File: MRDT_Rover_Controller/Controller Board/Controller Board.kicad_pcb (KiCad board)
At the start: 2 copper layers, 137.6 x 81.5 mm, 31 parts, among them Q1 S8050, SW1 EG1218, U1 MCP3008

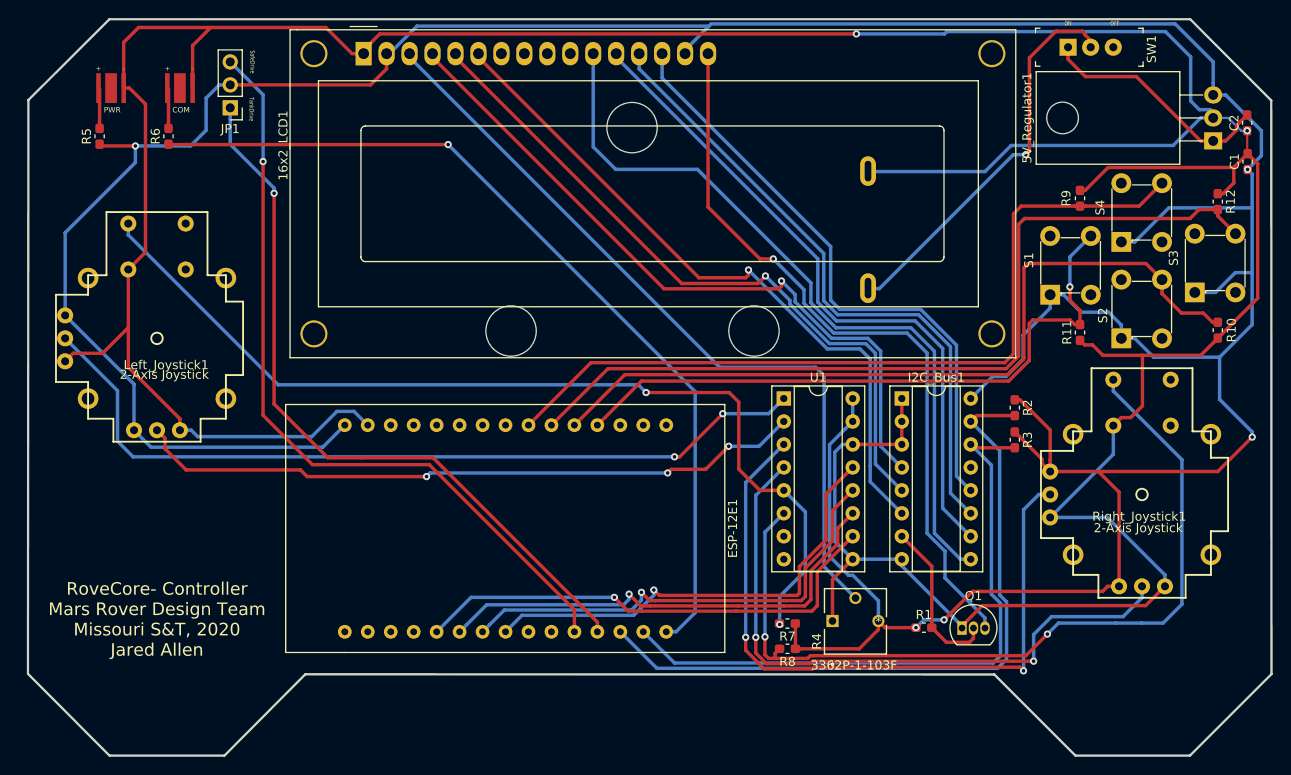
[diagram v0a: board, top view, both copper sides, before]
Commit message: All Push-Buttons Re-Mapped
Buttons 3 & 4 had to be re-mapped through the ADC due to compatability issues with the original pins they were connected to. All schematic and PCB changes have been made. Buttons 1 & 2 also needed to be re-mapped to account for the change, but are still connected to the ESP
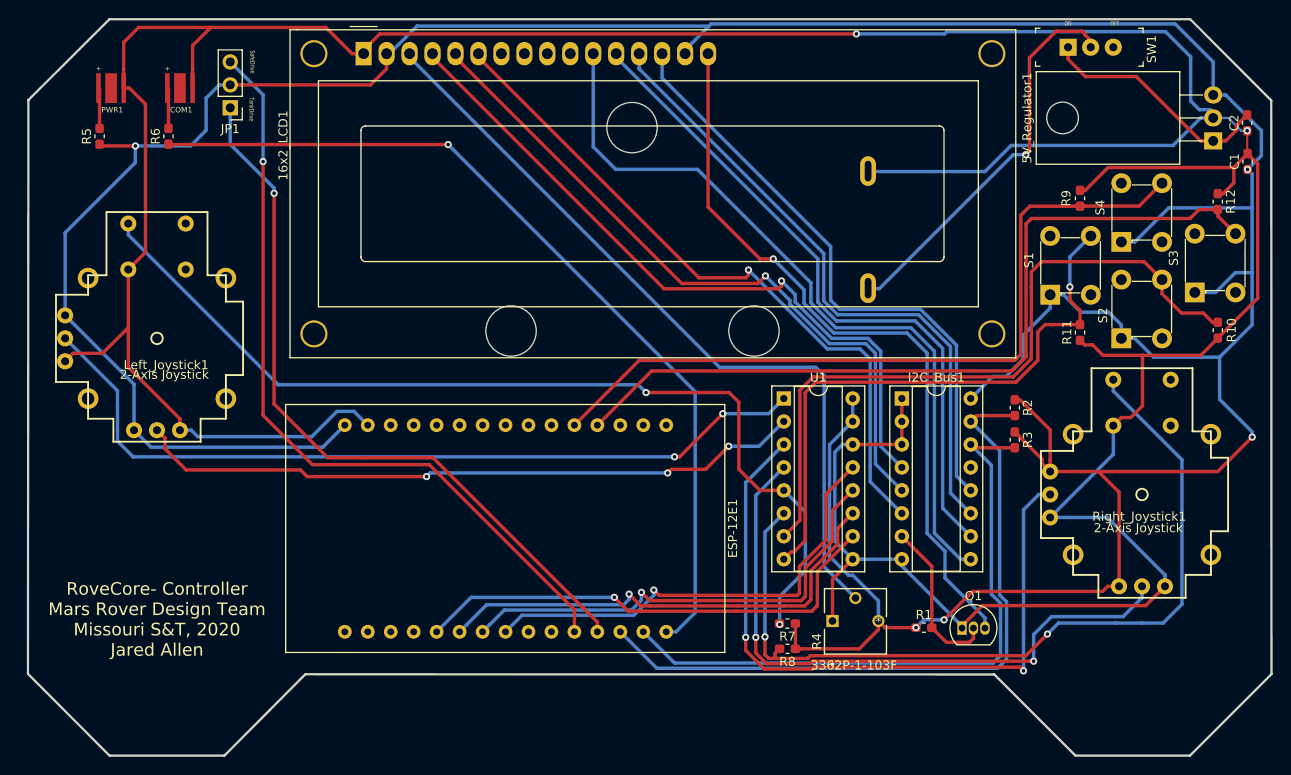
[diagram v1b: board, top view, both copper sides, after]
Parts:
- renumbered COM to COM1, PWR to PWR1
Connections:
- ESP-12E1 pad 11: SW3 -> Net-(ESP-12E1-Pad11)
- ESP-12E1 pad 13: SW4 -> Net-(ESP-12E1-Pad13)
- ESP-12E1 pad 7: SW1 -> SW3
- ESP-12E1 pad 9: SW2 -> SW4
- U1 pad 7: Net-(U1-Pad7) -> SW2
- U1 pad 8: Net-(U1-Pad8) -> SW1
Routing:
- net SW2: track 88.1 -> 78.3 mm
- net SW1: track 72.0 -> 66.2 mm
- net SW3: track 95.6 -> 90.6 mm
- net SW4: track 90.3 -> 85.7 mm

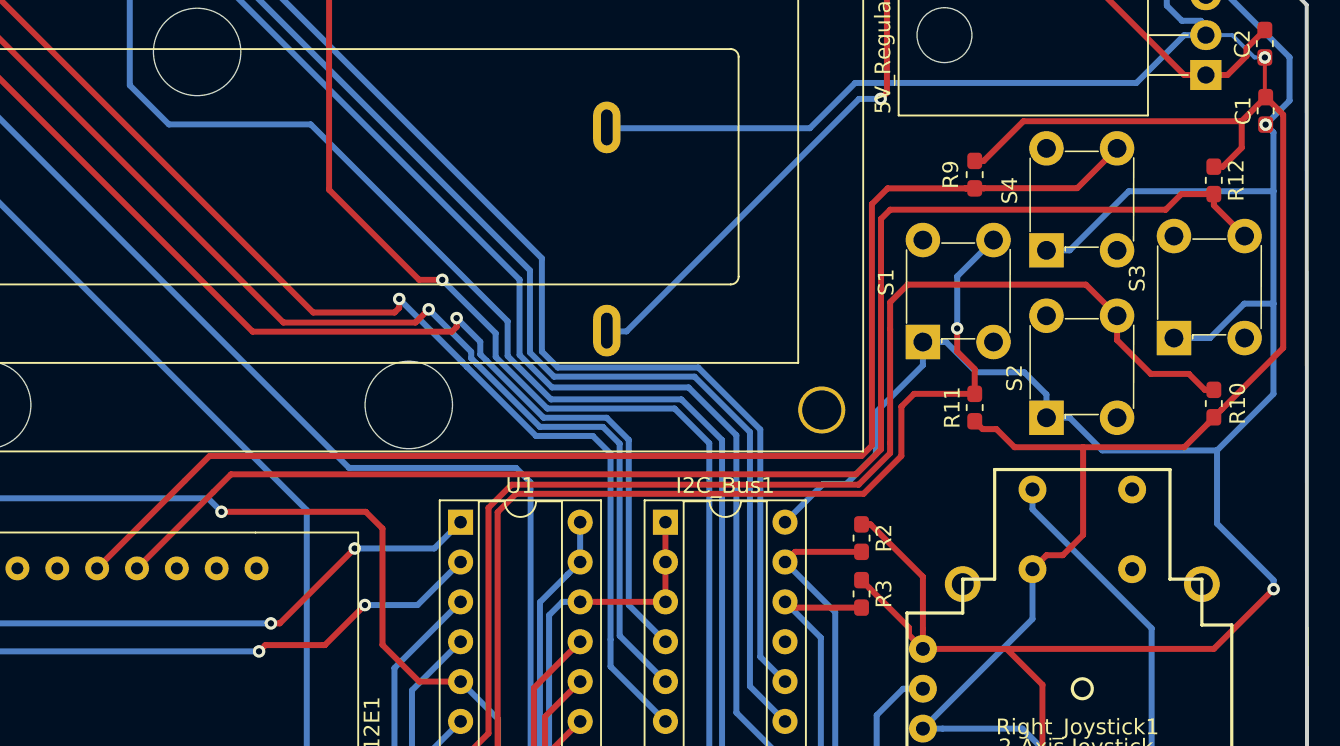
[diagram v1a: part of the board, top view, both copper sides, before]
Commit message: Button Resistor Connections Changed
Re-configuration to resistors connected to push buttons. Changes made for both schematic and PCB. All new traces placed.
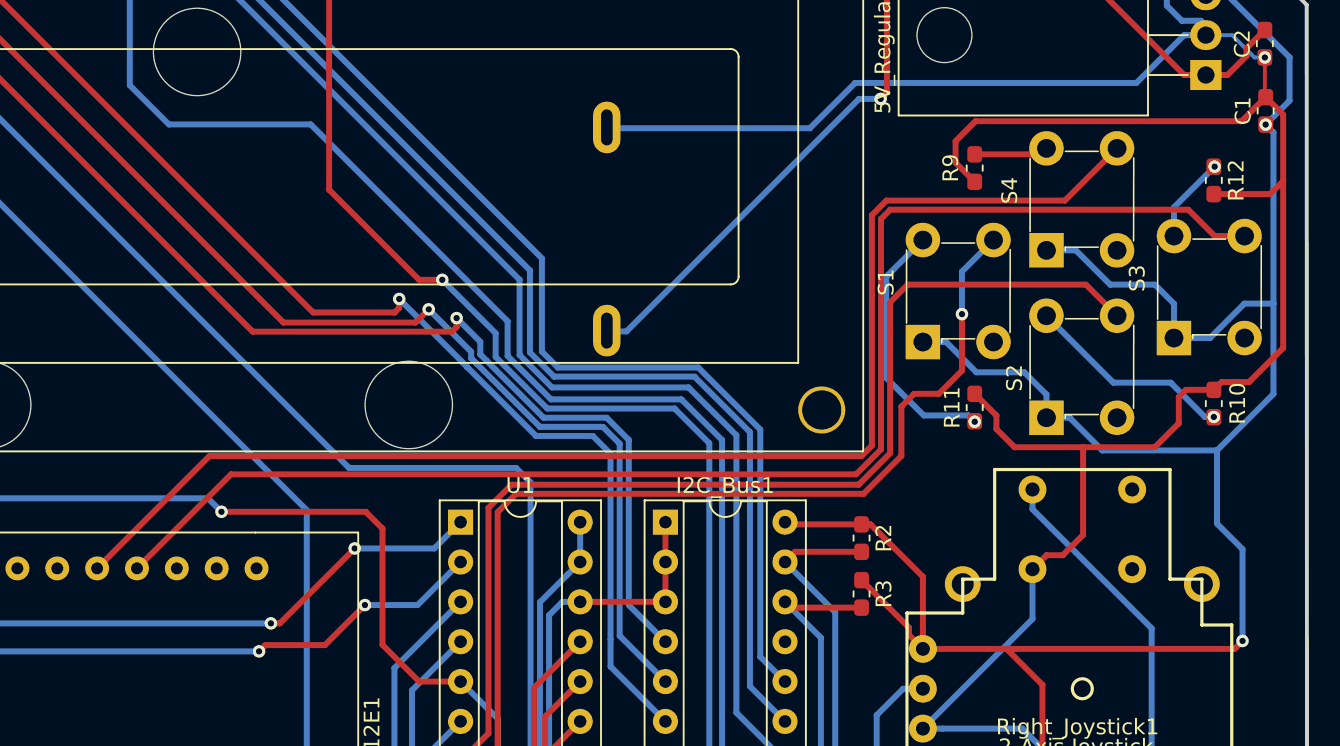
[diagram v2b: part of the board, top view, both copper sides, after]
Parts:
- R10, R11, R12, R9: value 100 -> 10K
- moved R9 0.42 mm to (192.3, 71.5)
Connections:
- R10 pad 1: GND -> Net-(R10-Pad1)
- R10 pad 2: SW2 -> GND
- R11 pad 1: GND -> Net-(R11-Pad1)
- R11 pad 2: SW1 -> GND
- R12 pad 1: GND -> Net-(R12-Pad1)
- R12 pad 2: SW3 -> GND
- R9 pad 1: GND -> Net-(R9-Pad1)
- R9 pad 2: SW4 -> GND
- S1 pad 2: Net-(S1-Pad2) -> Net-(R11-Pad1)
- S2 pad 2: Net-(S2-Pad2) -> Net-(R10-Pad1)
- S3 pad 2: Net-(S3-Pad2) -> Net-(R12-Pad1)
- S4 pad 2: Net-(S4-Pad2) -> Net-(R9-Pad1)
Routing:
- net Net-(R11-Pad1): track 0.00 -> 16.6 mm, vias 0 -> 1
- net 5V: track 435.7 -> 419.5 mm
- net Net-(R10-Pad1): track 0.00 -> 13.3 mm, vias 0 -> 1
- net SW2: track 78.3 -> 69.3 mm
- net GND: track 441.9 -> 448.7 mm
- net Net-(R12-Pad1): track 0.00 -> 5.50 mm, vias 0 -> 1
- net Net-(R9-Pad1): track 0.00 -> 4.73 mm
- net SW1: track 66.2 -> 63.9 mm
- net SW3: track 90.6 -> 89.4 mm
- net SW4: track 85.7 -> 84.7 mm

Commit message: Test Code Modifications
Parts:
- added G***: LOGO, MRDT_Silkscreens:0_MRDT_Logo_10mm, F.Cu at (92.5, 127.8)

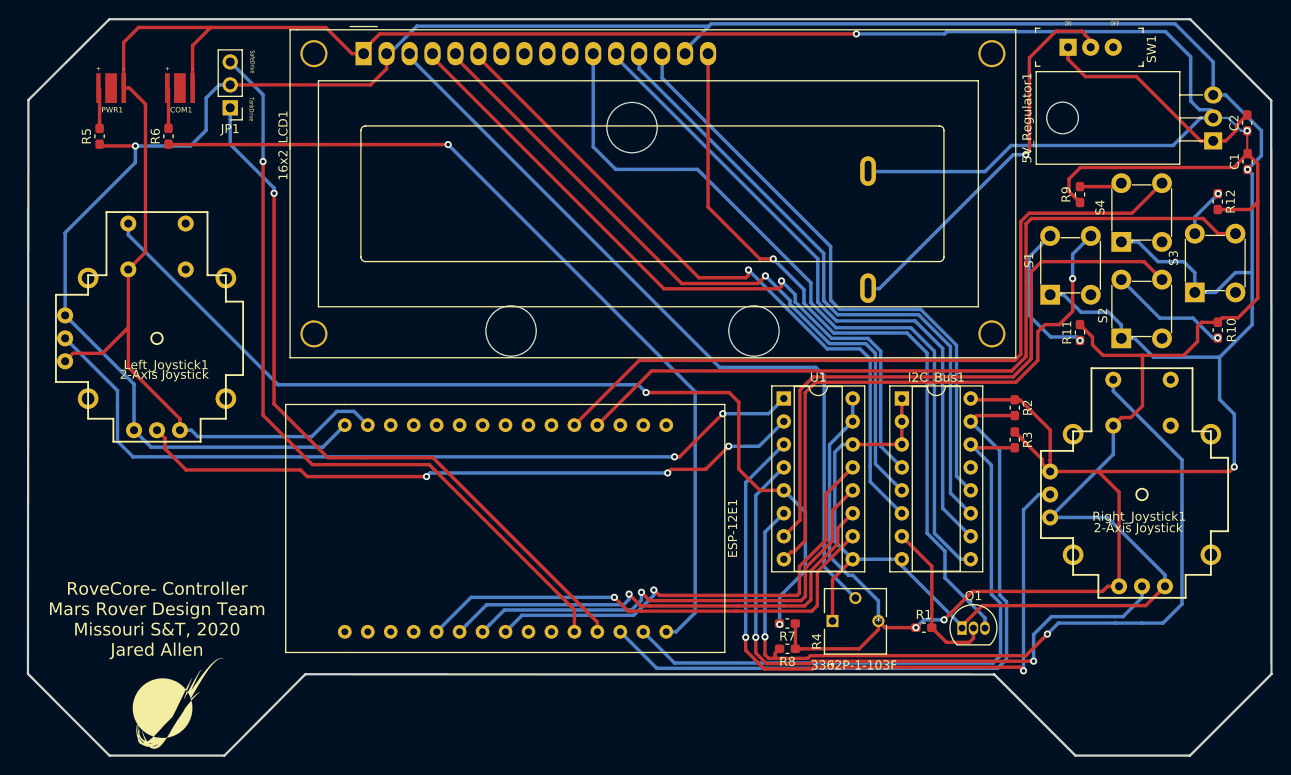
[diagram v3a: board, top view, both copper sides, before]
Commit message: Push Button and Jumper PCB Traces Updated
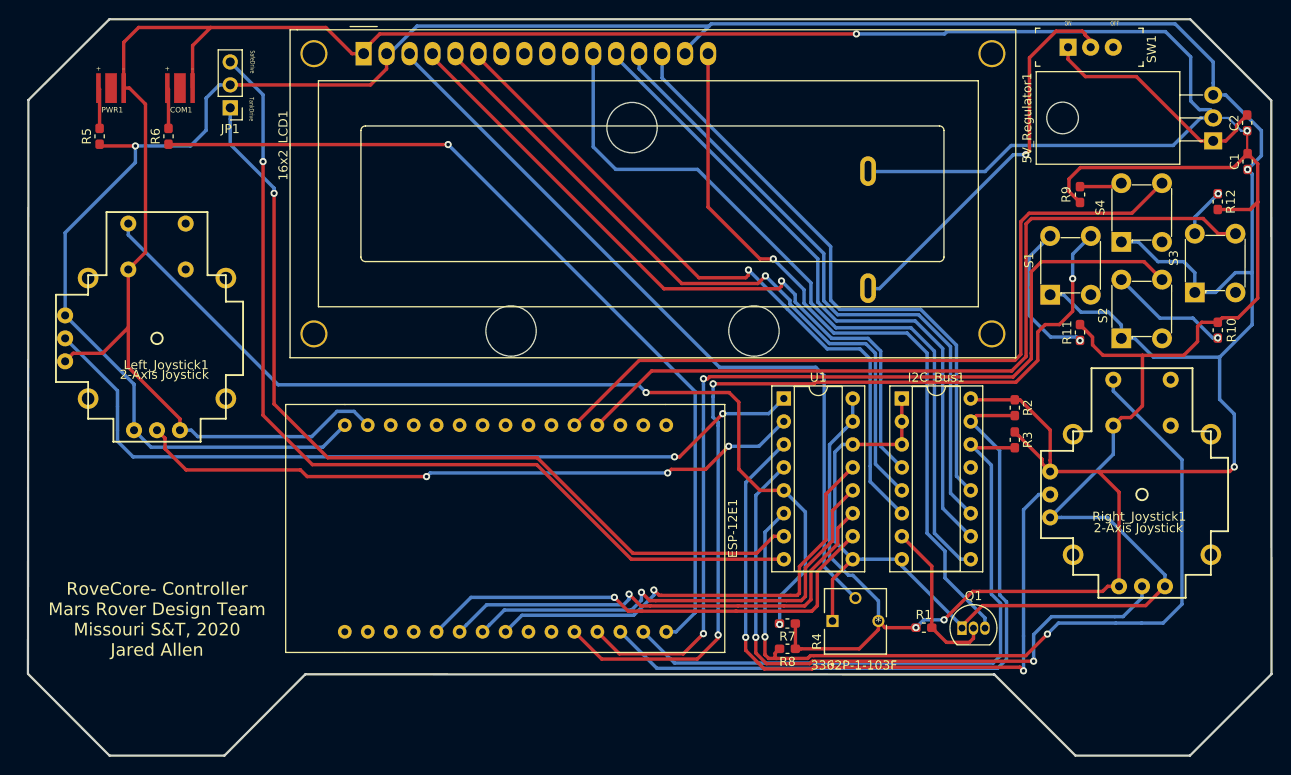
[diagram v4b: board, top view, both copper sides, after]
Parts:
- removed G***: LOGO, MRDT_Silkscreens:0_MRDT_Logo_10mm
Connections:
- ESP-12E1 pad 10: SafeDrive -> SW1
- ESP-12E1 pad 8: TankDrive -> SW2
- U1 pad 7: SW2 -> TankDrive
- U1 pad 8: SW1 -> SafeDrive
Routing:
- net SW1: track 63.9 -> 100.6 mm, vias 1 -> 3
- net SW2: track 69.3 -> 104.4 mm, vias 0 -> 2
- net SafeDrive: track 86.4 -> 104.8 mm
- net TankDrive: track 81.6 -> 98.8 mm

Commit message: New Button Traces Placed
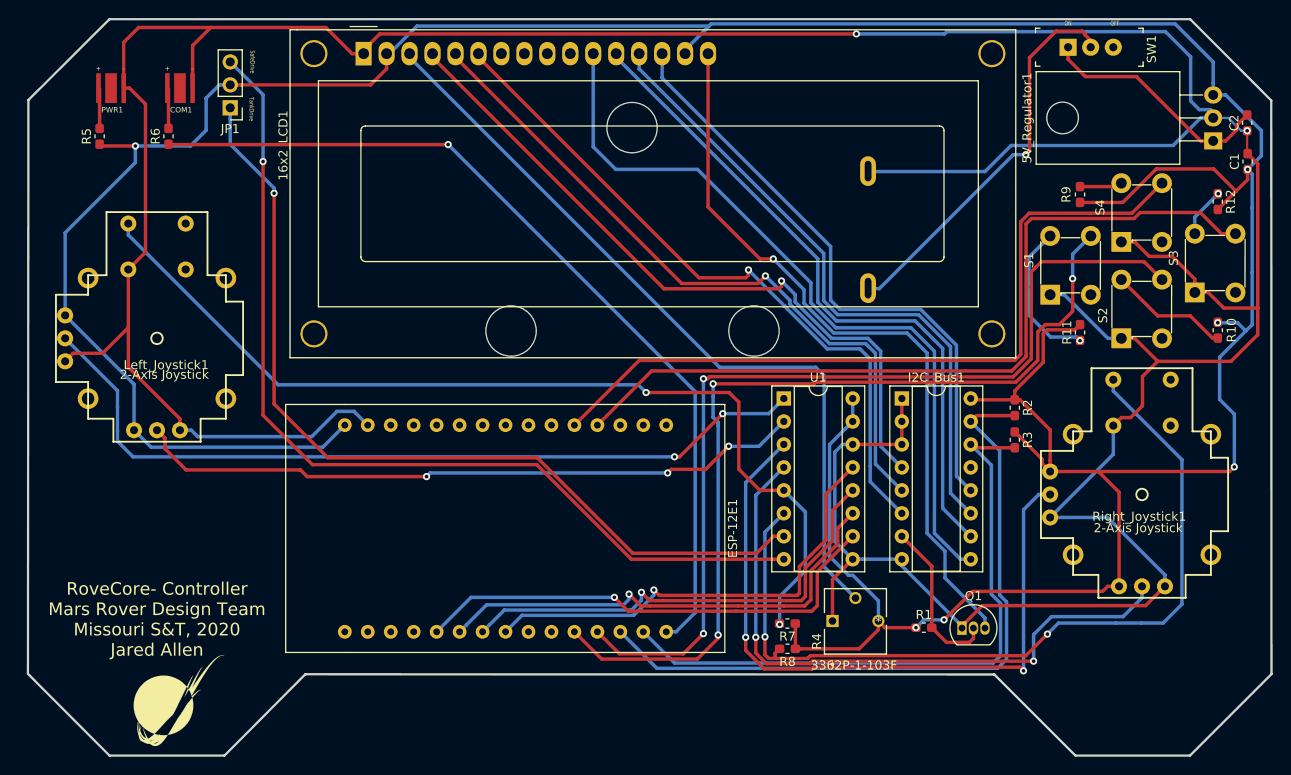
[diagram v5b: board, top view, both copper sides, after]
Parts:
- added G***: LOGO, MRDT_Silkscreens:0_MRDT_Logo_10mm, F.Cu at (92.6, 127.5)
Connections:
- R10 pad 2: GND -> 5V
- R11 pad 2: GND -> 5V
- R12 pad 2: GND -> 5V
- R9 pad 2: GND -> 5V
- S1 pad 1: 5V -> GND
- S2 pad 1: 5V -> GND
- S3 pad 1: 5V -> GND
- S4 pad 1: 5V -> GND
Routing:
- net GND: track 448.7 -> 445.6 mm
- net SW3: track 89.4 -> 89.9 mm
- net 5V: track 419.5 -> 419.7 mm, vias 5 -> 6
- net Net-(R10-Pad1): vias 1 -> 0

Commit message: 3D Files Updated
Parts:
- renumbered U1 to ADC1
